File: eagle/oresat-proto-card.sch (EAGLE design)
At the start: 99 parts, among them J1 J-SAMTEC-TFM-110-X1-XXX-D-RA, J2 U.FL, J3 U.FL, J4 U.FL, J6 J-SAMTEC-TFM-120-X1-XXX-D-RA, J7 1.27MM-SWD-CONNECTOR, Q3 MOSFET-PCH-SOT23-6, Q4 MOSFET-PCH-SOT23-6, Q5 PMV45EN, Q6 PMV45EN, U2 TCAN330, U3 MAX7310, U4 MAX4211, U5 TPS62111, U6 STM32F042K6, X1 16MHZ-2.5x2mm

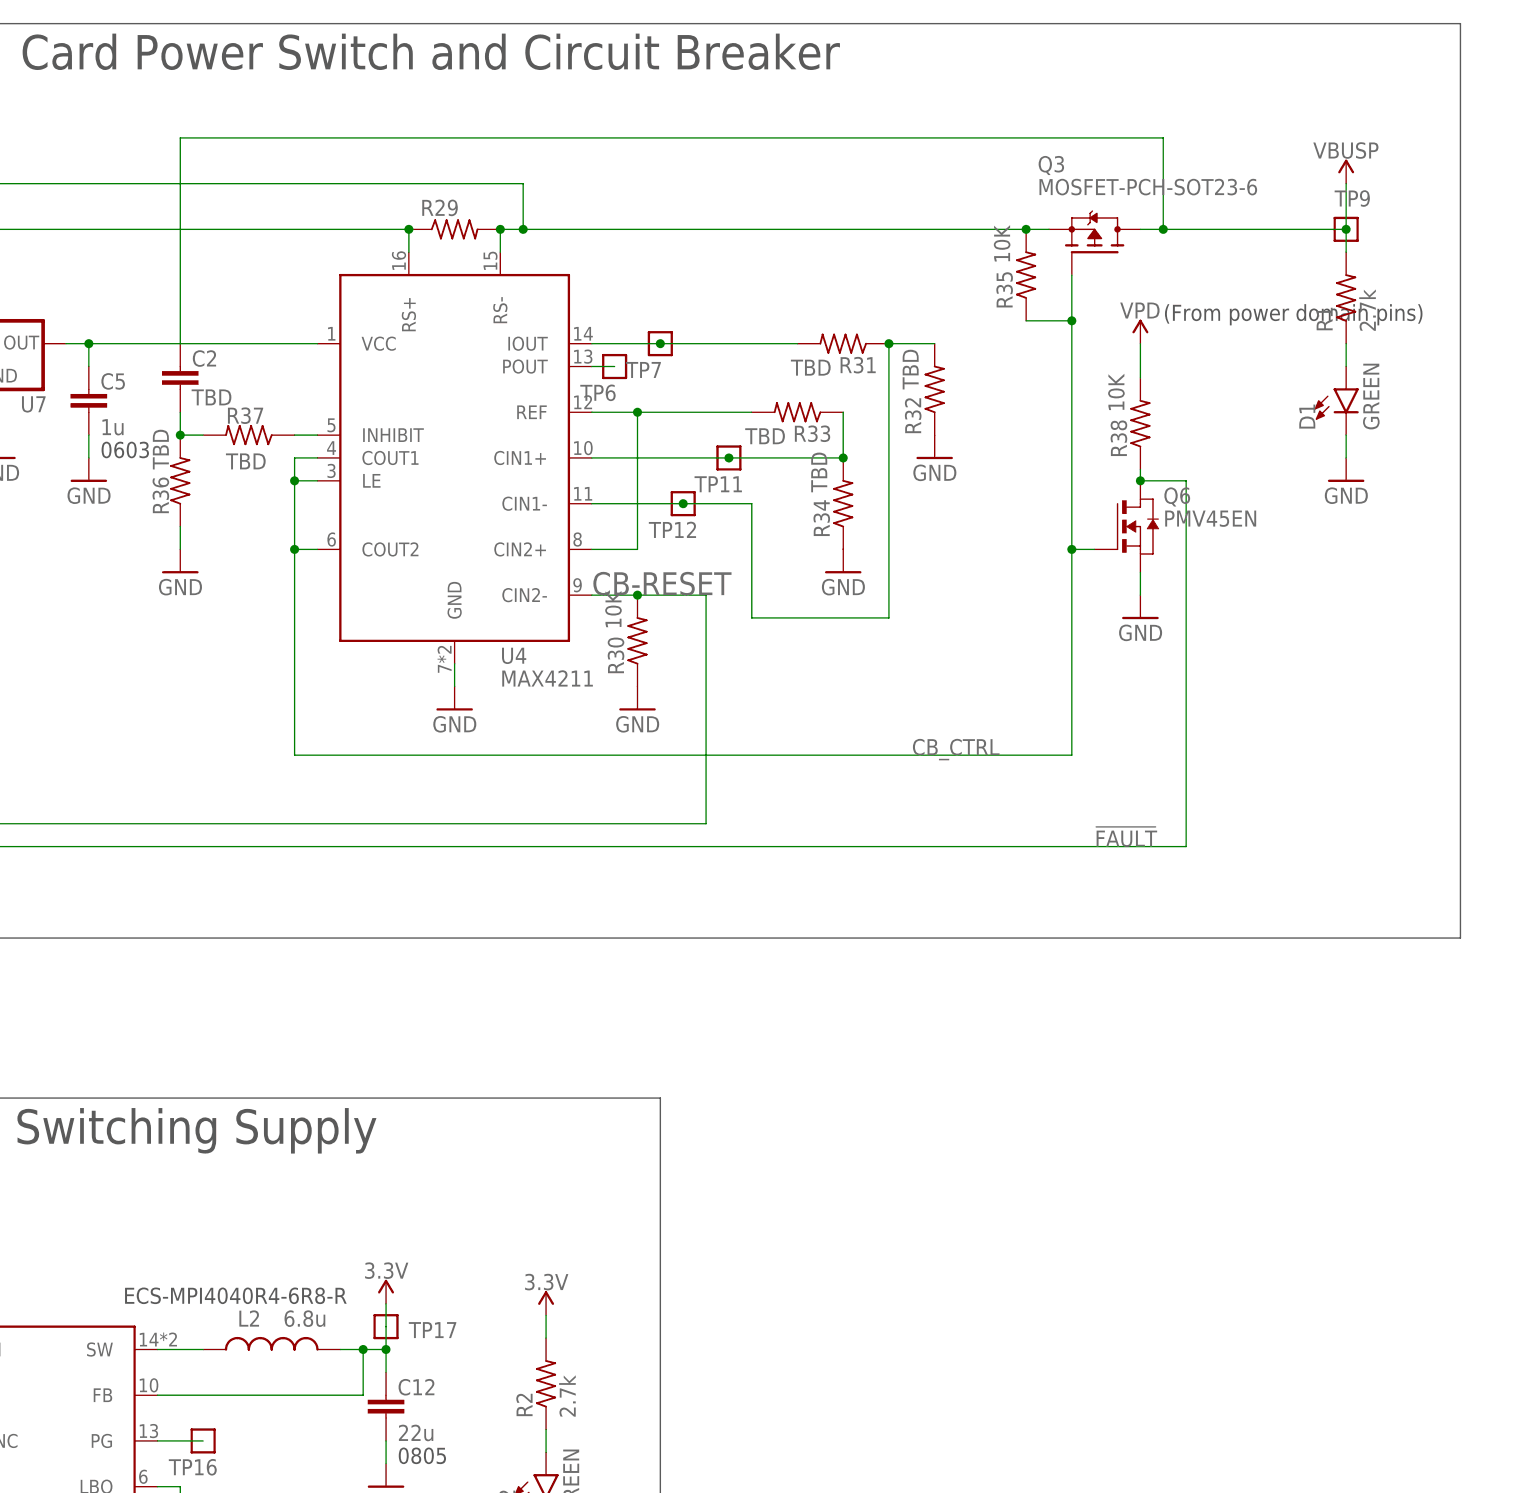
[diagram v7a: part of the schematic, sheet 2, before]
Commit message: More schematic and board polishing. Went over ERCs and DRCs, some layout polishing, more ground stitching.
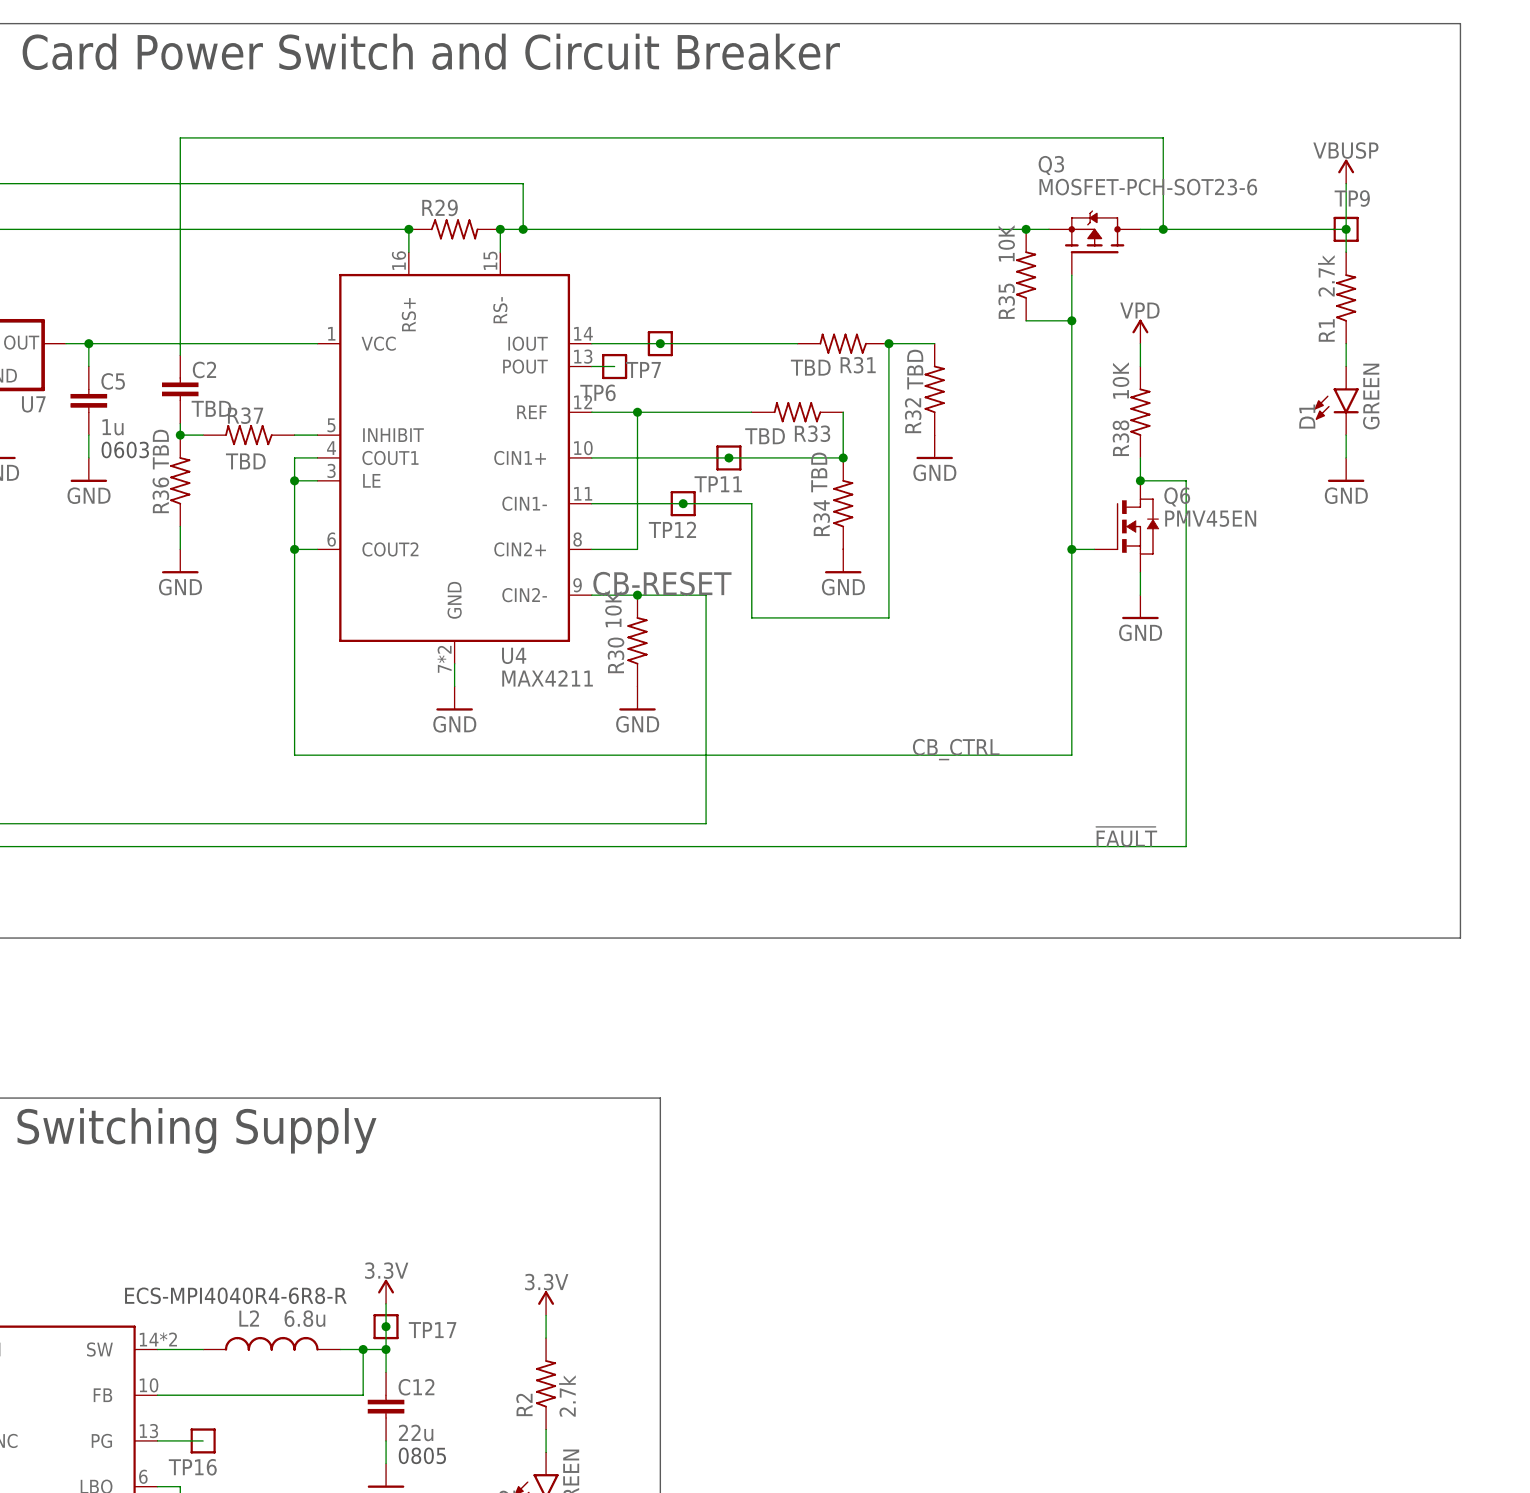
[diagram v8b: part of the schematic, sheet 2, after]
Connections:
- net N$585 renamed MAX4211-3V3
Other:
- note removed: "(From power domain pins)"
- moved on the sheet: C2, R38
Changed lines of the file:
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@@
 <?xml version="1.0" encoding="utf-8"?>
 <!DOCTYPE eagle SYSTEM "eagle.dtd">
-<eagle version="9.2.2">
+<eagle version="9.3.0">
 <drawing>
 <settings>
@@
 <setting verticaltext="up"/>
 </settings>
-<grid distance="0.1" unitdist="inch" unit="inch" style="lines" multiple="1" display="no" altdistance="0.01" altunitdist="inch" altunit="inch"/>
+<grid distance="0.05" unitdist="inch" unit="inch" style="lines" multiple="2" display="yes" altdistance="0.01" altunitdist="inch" altunit="inch"/>
 <layers>
 <layer number="1" name="Top" color="4" fill="1" visible="no" active="no"/>
@@
 <text x="64.77" y="96.52" size="1.778" layer="97">OreSat Power Domain (OPD)
 Power Supply (3.3V)</text>
-<text x="363.22" y="187.96" size="1.778" layer="97">(From power domain pins)</text>
 <text x="40.64" y="215.9" size="3.81" layer="97">OreSat Power Domain (OPD) Controller</text>
 <wire x1="22.86" y1="220.98" x2="157.48" y2="220.98" width="0.1524" layer="97"/>
@@
 <attribute name="MFR" x="383.54" y="190.5" size="1.778" layer="96" rot="R90" display="off"/>
 <attribute name="MPN" x="383.54" y="190.5" size="1.778" layer="96" rot="R90" display="off"/>
-<attribute name="NAME" x="382.0414" y="186.69" size="1.778" layer="95" rot="R90"/>
-<attribute name="VALUE" x="386.842" y="186.69" size="1.778" layer="96" rot="R90"/>
+<attribute name="NAME" x="382.27" y="185.42" size="1.778" layer="95" rot="R90"/>
+<attribute name="VALUE" x="382.27" y="190.5" size="1.778" layer="96" rot="R90"/>
 </instance>
 <instance part="R2" gate="R" x="294.64" y="69.85" smashed="yes" rot="R90">
@@
 <attribute name="MPN" x="337.82" y="180.34" size="1.778" layer="96" rot="R90" display="off"/>
 <attribute name="NAME" x="336.3214" y="175.26" size="1.778" layer="95" rot="R90"/>
-<attribute name="VALUE" x="336.042" y="180.34" size="1.778" layer="96" rot="R90"/>
+<attribute name="VALUE" x="336.55" y="180.34" size="1.778" layer="96" rot="R90"/>
 </instance>
 <instance part="R33" gate="R" x="322.58" y="177.8" smashed="yes" rot="R180">
@@
 <attribute name="MFR" x="347.98" y="193.04" size="1.778" layer="96" rot="R90" display="off"/>
 <attribute name="MPN" x="347.98" y="193.04" size="1.778" layer="96" rot="R90" display="off"/>
-<attribute name="NAME" x="346.4814" y="189.23" size="1.778" layer="95" rot="R90"/>
-<attribute name="VALUE" x="346.202" y="194.31" size="1.778" layer="96" rot="R90"/>
+<attribute name="NAME" x="346.71" y="187.96" size="1.778" layer="95" rot="R90"/>
+<attribute name="VALUE" x="346.71" y="194.31" size="1.778" layer="96" rot="R90"/>
 </instance>
 <instance part="R36" gate="R" x="254" y="170.18" smashed="yes" rot="R90">
@@
 <attribute name="VALUE" x="256.54" y="157.48" size="1.778" layer="96" rot="MR0"/>
 </instance>
-<instance part="C2" gate="CE" x="254" y="180.34" smashed="yes" rot="MR180">
-<attribute name="DIS" x="254" y="180.34" size="1.778" layer="96" rot="MR180" display="off"/>
-<attribute name="DPN" x="254" y="180.34" size="1.778" layer="96" rot="MR180" display="off"/>
-<attribute name="MFR" x="254" y="180.34" size="1.778" layer="96" rot="MR180" display="off"/>
-<attribute name="MPN" x="254" y="180.34" size="1.778" layer="96" rot="MR180" display="off"/>
-<attribute name="NAME" x="255.27" y="182.88" size="1.778" layer="95"/>
-<attribute name="VALUE" x="255.27" y="180.34" size="1.778" layer="96" rot="MR180"/>
+<instance part="C2" gate="CE" x="254" y="179.07" smashed="yes" rot="MR180">
+<attribute name="DIS" x="254" y="179.07" size="1.778" layer="96" rot="MR180" display="off"/>
+<attribute name="DPN" x="254" y="179.07" size="1.778" layer="96" rot="MR180" display="off"/>
+<attribute name="MFR" x="254" y="179.07" size="1.778" layer="96" rot="MR180" display="off"/>
+<attribute name="MPN" x="254" y="179.07" size="1.778" layer="96" rot="MR180" display="off"/>
+<attribute name="NAME" x="255.27" y="181.61" size="1.778" layer="95"/>
+<attribute name="VALUE" x="255.27" y="179.07" size="1.778" layer="96" rot="MR180"/>
 </instance>
 <instance part="GND37" gate="1" x="360.68" y="154.94" smashed="yes" rot="MR0">
 <attribute name="VALUE" x="363.22" y="152.4" size="1.778" layer="96" rot="MR0"/>
 </instance>
-<instance part="R38" gate="R" x="360.68" y="176.53" smashed="yes" rot="R90">
-<attribute name="DIS" x="360.68" y="176.53" size="1.778" layer="96" rot="R90" display="off"/>
-<attribute name="DPN" x="360.68" y="176.53" size="1.778" layer="96" rot="R90" display="off"/>
-<attribute name="MFR" x="360.68" y="176.53" size="1.778" layer="96" rot="R90" display="off"/>
-<attribute name="MPN" x="360.68" y="176.53" size="1.778" layer="96" rot="R90" display="off"/>
-<attribute name="NAME" x="359.1814" y="172.72" size="1.778" layer="95" rot="R90"/>
-<attribute name="VALUE" x="358.902" y="177.8" size="1.778" layer="96" rot="R90"/>
+<instance part="R38" gate="R" x="360.68" y="177.8" smashed="yes" rot="R90">
+<attribute name="DIS" x="360.68" y="177.8" size="1.778" layer="96" rot="R90" display="off"/>
+<attribute name="DPN" x="360.68" y="177.8" size="1.778" layer="96" rot="R90" display="off"/>
+<attribute name="MFR" x="360.68" y="177.8" size="1.778" layer="96" rot="R90" display="off"/>
+<attribute name="MPN" x="360.68" y="177.8" size="1.778" layer="96" rot="R90" display="off"/>
+<attribute name="NAME" x="359.41" y="172.72" size="1.778" layer="95" rot="R90"/>
+<attribute name="VALUE" x="359.41" y="179.07" size="1.778" layer="96" rot="R90"/>
 </instance>
 <instance part="TP8" gate="G$1" x="203.2" y="129.54" smashed="yes">
@@
 <pinref part="TP17" gate="G$1" pin="1"/>
 <pinref part="L2" gate="G$1" pin="2"/>
+<junction x="276.86" y="76.2"/>
 </segment>
 </net>
@@
 <wire x1="254" y1="175.26" x2="256.54" y2="175.26" width="0.1524" layer="91"/>
 <pinref part="C2" gate="CE" pin="1"/>
-<wire x1="254" y1="177.8" x2="254" y2="175.26" width="0.1524" layer="91"/>
+<wire x1="254" y1="176.53" x2="254" y2="175.26" width="0.1524" layer="91"/>
 <junction x="254" y="175.26"/>
 </segment>
@@
 <pinref part="TP8" gate="G$1" pin="1"/>
 <junction x="203.2" y="129.54"/>
-<wire x1="360.68" y1="171.45" x2="360.68" y2="170.18" width="0.1524" layer="91"/>
+<wire x1="360.68" y1="172.72" x2="360.68" y2="170.18" width="0.1524" layer="91"/>
 <label x="144.78" y="139.7" size="1.778" layer="95"/>
 <label x="355.6" y="129.54" size="1.778" layer="95"/>
@@
 </segment>
 </net>
-<net name="N$585" class="0">
+<net name="MAX4211-3V3" class="0">
 <segment>
 <pinref part="C5" gate="CE" pin="1"/>
@@
 <wire x1="383.54" y1="203.2" x2="383.54" y2="198.12" width="0.1524" layer="91"/>
 <pinref part="C2" gate="CE" pin="2"/>
-<wire x1="254" y1="185.42" x2="254" y2="208.28" width="0.1524" layer="91"/>
+<wire x1="254" y1="184.15" x2="254" y2="208.28" width="0.1524" layer="91"/>
 <wire x1="254" y1="208.28" x2="363.22" y2="208.28" width="0.1524" layer="91"/>
 <wire x1="363.22" y1="208.28" x2="363.22" y2="198.12" width="0.1524" layer="91"/>
@@
 <pinref part="R38" gate="R" pin="2"/>
 <pinref part="VPD1" gate="G$1" pin="VPD"/>
-<wire x1="360.68" y1="185.42" x2="360.68" y2="181.61" width="0.1524" layer="91"/>
-</segment>
-<segment>
+<wire x1="360.68" y1="185.42" x2="360.68" y2="182.88" width="0.1524" layer="91"/>
+</segment>
+<segment>
